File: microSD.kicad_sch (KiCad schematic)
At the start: 3 parts, among them J16 Micro_SD_Card_Det

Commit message: commit
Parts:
- added JP31: SolderJumper_2_Open, iclr:SmallerSolderJP, symbol Jumper:SolderJumper_2_Open
- added Q1: PMOS, Package_TO_SOT_SMD:SOT-723, symbol Simulation_SPICE:PMOS
- added R39: 1k, Resistor_SMD:R_0402_1005Metric, symbol Device:R_Small
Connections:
- net +3V3: now also JP31.1 (A), Q1.3 (S); no longer C10.1, J16.4 (VDD)
- net GND: now also R39.1
- new net: C10.1, J16.4 (VDD), JP31.2 (B), Q1.1 (D)
- new net SD_Pow: Q1.2 (G), R39.2
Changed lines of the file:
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@@
 (kicad_sch (version 20230121) (generator eeschema)
   (paper "A4")
+  (junction (at 108.204 59.69) (diameter 0) (color 0 0 0 0)
+  )
+  (junction (at 99.822 54.102) (diameter 0) (color 0 0 0 0)
+  )
   (junction (at 104.902 101.6) (diameter 0) (color 0 0 0 0)
   )
   (junction (at 99.822 66.04) (diameter 0) (color 0 0 0 0)
+  )
+  (junction (at 99.822 64.77) (diameter 0) (color 0 0 0 0)
   )
   (no_connect (at 116.332 83.82))
   (no_connect (at 116.332 66.04))
+  (wire (pts (xy 99.822 64.77) (xy 87.376 64.77))
+    (stroke (width 0) (type default))
+  )
+  (wire (pts (xy 87.376 54.102) (xy 99.822 54.102))
+    (stroke (width 0) (type default))
+  )
   (wire (pts (xy 115.062 68.58) (xy 116.332 68.58))
     (stroke (width 0) (type default))
@@
     (stroke (width 0) (type default))
   )
+  (wire (pts (xy 87.376 56.134) (xy 87.376 54.102))
+    (stroke (width 0) (type default))
+  )
   (wire (pts (xy 99.822 66.04) (xy 99.822 73.66))
     (stroke (width 0) (type default))
@@
     (stroke (width 0) (type default))
   )
+  (wire (pts (xy 99.822 53.086) (xy 99.822 54.102))
+    (stroke (width 0) (type default))
+  )
   (wire (pts (xy 101.092 101.6) (xy 104.902 101.6))
     (stroke (width 0) (type default))
@@
     (stroke (width 0) (type default))
   )
+  (wire (pts (xy 107.442 59.69) (xy 108.204 59.69))
+    (stroke (width 0) (type default))
+  )
   (wire (pts (xy 108.712 86.36) (xy 108.712 101.6))
     (stroke (width 0) (type default))
@@
     (stroke (width 0) (type default))
   )
+  (wire (pts (xy 108.204 59.69) (xy 109.347 59.69))
+    (stroke (width 0) (type default))
+  )
+  (wire (pts (xy 87.376 64.77) (xy 87.376 63.754))
+    (stroke (width 0) (type default))
+  )
+  (wire (pts (xy 99.822 54.102) (xy 99.822 54.61))
+    (stroke (width 0) (type default))
+  )
   (wire (pts (xy 159.512 88.9) (xy 162.052 88.9))
     (stroke (width 0) (type default))
+  )
+  (hierarchical_label "SD_Pow" (shape input) (at 109.347 59.69 0) (fields_autoplaced)
+    (effects (font (size 1.27 1.27)) (justify left))
   )
   (hierarchical_label "VSPI_SCLK" (shape input) (at 115.062 76.2 180) (fields_autoplaced)
@@
     )
   )
+  (symbol (lib_id "power:GND") (at 108.204 64.77 0) (unit 1)
+    (in_bom yes) (on_board yes) (dnp no) (fields_autoplaced)
+    (property "Reference" "#PWR085" (at 108.204 71.12 0)
+      (effects (font (size 1.27 1.27)) hide)
+    )
+    (property "Value" "GND" (at 110.109 66.4738 0)
+      (effects (font (size 1.27 1.27)) (justify left) hide)
+    )
+    (property "Footprint" "" (at 108.204 64.77 0)
+      (effects (font (size 1.27 1.27)) hide)
+    )
+    (property "Datasheet" "" (at 108.204 64.77 0)
+      (effects (font (size 1.27 1.27)) hide)
+    )
+    (pin "1")
+    (instances
+      (project "Ricardo-Stark"
+        (path "/7db990e4-92e1-4f99-b4d2-435bbec1ba83/cbb4aecb-b4d4-4eab-8e16-74accf8129be"
+          (reference "#PWR030") (unit 1)
+        )
+      )
+    )
+  )
   (symbol (lib_id "power:+3.3V") (at 104.902 92.71 0) (unit 1)
     (in_bom yes) (on_board yes) (dnp no) (fields_autoplaced)
@@
     )
   )
-  (symbol (lib_id "power:+3.3V") (at 99.822 64.77 0) (unit 1)
-    (in_bom yes) (on_board yes) (dnp no) (fields_autoplaced)
-    (property "Reference" "#PWR0157" (at 99.822 68.58 0)
-      (effects (font (size 1.27 1.27)) hide)
-    )
-    (property "Value" "+3.3V" (at 99.822 59.69 0)
-      (effects (font (size 1.27 1.27)))
-    )
-    (property "Footprint" "" (at 99.822 64.77 0)
-      (effects (font (size 1.27 1.27)) hide)
-    )
-    (property "Datasheet" "" (at 99.822 64.77 0)
-      (effects (font (size 1.27 1.27)) hide)
-    )
-    (pin "1")
-    (instances
-      (project "sensorboard"
-        (path "/26801cfb-b53b-4a6a-a2f4-5f4986565765/f50ea3f6-9887-4dc3-9ec9-7a0fb1ee7721"
-          (reference "#PWR0157") (unit 1)
-        )
-      )
-      (project "Ricardo-Stark"
-        (path "/7db990e4-92e1-4f99-b4d2-435bbec1ba83/cbb4aecb-b4d4-4eab-8e16-74accf8129be"
-          (reference "#PWR0169") (unit 1)
+  (symbol (lib_id "Jumper:SolderJumper_2_Open") (at 87.376 59.944 270) (unit 1)
+    (in_bom yes) (on_board yes) (dnp no)
+    (property "Reference" "JP31" (at 82.296 59.944 0)
+      (effects (font (size 1.27 1.27)))
+    )
+    (property "Value" "SolderJumper_2_Open" (at 55.626 42.164 0)
+      (effects (font (size 1.27 1.27)) hide)
+    )
+    (property "Footprint" "iclr:SmallerSolderJP" (at 87.376 59.944 0)
+      (effects (font (size 1.27 1.27)) hide)
+    )
+    (property "Datasheet" "~" (at 87.376 59.944 0)
+      (effects (font (size 1.27 1.27)) hide)
+    )
+    (pin "1")
+    (pin "2")
+    (instances
+      (project "sensorboard - Copy"
+        (path "/26801cfb-b53b-4a6a-a2f4-5f4986565765/00000000-0000-0000-0000-000061b9f0c0"
+          (reference "JP31") (unit 1)
+        )
+      )
+      (project "Ricardo-Stark"
+        (path "/7db990e4-92e1-4f99-b4d2-435bbec1ba83/249a9f46-b59f-4de1-97d1-386ac76339a5"
+          (reference "JP27") (unit 1)
+        )
+        (path "/7db990e4-92e1-4f99-b4d2-435bbec1ba83/cbb4aecb-b4d4-4eab-8e16-74accf8129be"
+          (reference "JP3") (unit 1)
         )
       )
@@
         )
       )
+    )
+  )
+  (symbol (lib_id "power:+3.3V") (at 99.822 53.086 0) (unit 1)
+    (in_bom yes) (on_board yes) (dnp no) (fields_autoplaced)
+    (property "Reference" "#PWR0159" (at 99.822 56.896 0)
+      (effects (font (size 1.27 1.27)) hide)
+    )
+    (property "Value" "+3.3V" (at 99.822 48.006 0)
+      (effects (font (size 1.27 1.27)))
+    )
+    (property "Footprint" "" (at 99.822 53.086 0)
+      (effects (font (size 1.27 1.27)) hide)
+    )
+    (property "Datasheet" "" (at 99.822 53.086 0)
+      (effects (font (size 1.27 1.27)) hide)
+    )
+    (pin "1")
+    (instances
+      (project "sensorboard"
+        (path "/26801cfb-b53b-4a6a-a2f4-5f4986565765/f50ea3f6-9887-4dc3-9ec9-7a0fb1ee7721"
+          (reference "#PWR0159") (unit 1)
+        )
+      )
+      (project "Ricardo-Stark"
+        (path "/7db990e4-92e1-4f99-b4d2-435bbec1ba83/cbb4aecb-b4d4-4eab-8e16-74accf8129be"
+          (reference "#PWR031") (unit 1)
+        )
+      )
+    )
+  )
+  (symbol (lib_id "Device:R_Small") (at 108.204 62.23 180) (unit 1)
+    (in_bom yes) (on_board yes) (dnp no)
+    (property "Reference" "R39" (at 104.775 62.3601 0)
+      (effects (font (size 1.27 1.27)))
+    )
+    (property "Value" "1k" (at 104.775 64.897 0)
+      (effects (font (size 1.27 1.27)))
+    )
+    (property "Footprint" "Resistor_SMD:R_0402_1005Metric" (at 108.204 62.23 0)
+      (effects (font (size 1.27 1.27)) hide)
+    )
+    (property "Datasheet" "~" (at 108.204 62.23 0)
+      (effects (font (size 1.27 1.27)) hide)
+    )
+    (pin "1")
+    (pin "2")
+    (instances
+      (project "Ricardo-Stark"
+        (path "/7db990e4-92e1-4f99-b4d2-435bbec1ba83/cbb4aecb-b4d4-4eab-8e16-74accf8129be"
+          (reference "R14") (unit 1)
+        )
+      )
+    )
+  )
+  (symbol (lib_id "Simulation_SPICE:PMOS") (at 102.362 59.69 180) (unit 1)
+    (in_bom yes) (on_board yes) (dnp no) (fields_autoplaced)
+    (property "Reference" "Q1" (at 96.012 58.42 0)
+      (effects (font (size 1.27 1.27)) (justify left))
+    )
+    (property "Value" "PMOS" (at 96.012 60.96 0)
+      (effects (font (size 1.27 1.27)) (justify left))
+    )
+    (property "Footprint" "Package_TO_SOT_SMD:SOT-723" (at 97.282 62.23 0)
+      (effects (font (size 1.27 1.27)) hide)
+    )
+    (property "Datasheet" "https://ngspice.sourceforge.io/docs/ngspice-manual.pdf" (at 102.362 46.99 0)
+      (effects (font (size 1.27 1.27)) hide)
+    )
+    (property "Sim.Device" "PMOS" (at 102.362 42.545 0)
+      (effects (font (size 1.27 1.27)) hide)
+    )
+    (property "Sim.Type" "VDMOS" (at 102.362 40.64 0)
+      (effects (font (size 1.27 1.27)) hide)
+    )
+    (property "Sim.Pins" "1=D 2=G 3=S" (at 102.362 44.45 0)
+      (effects (font (size 1.27 1.27)) hide)
+    )
+    (pin "2")
+    (pin "3")
+    (pin "1")
+    (instances
+      (project "Ricardo-Stark"
+        (path "/7db990e4-92e1-4f99-b4d2-435bbec1ba83/cbb4aecb-b4d4-4eab-8e16-74accf8129be"
+          (reference "Q1") (unit 1)
+        )
+      )

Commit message: added silkscreen
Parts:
- renumbered R39 to R14
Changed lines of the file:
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@@
   (symbol (lib_id "power:GND") (at 108.204 64.77 0) (unit 1)
     (in_bom yes) (on_board yes) (dnp no) (fields_autoplaced)
-    (property "Reference" "#PWR085" (at 108.204 71.12 0)
+    (property "Reference" "#PWR030" (at 108.204 71.12 0)
       (effects (font (size 1.27 1.27)) hide)
     )
@@
   (symbol (lib_id "Device:R_Small") (at 108.204 62.23 180) (unit 1)
     (in_bom yes) (on_board yes) (dnp no)
-    (property "Reference" "R39" (at 104.775 62.3601 0)
-      (effects (font (size 1.27 1.27)))
-    )
+    (property "Reference" "R14" (at 104.775 62.3601 0)
+      (effects (font (size 1.27 1.27)))
+    )

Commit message: changed sd mosfet footprint
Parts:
- Q1: footprint Package_TO_SOT_SMD:SOT-723 -> Package_TO_SOT_SMD:TSOT-23
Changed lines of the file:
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@@
 			)
 		)
-		(property "Footprint" "Package_TO_SOT_SMD:SOT-723"
+		(property "Footprint" "Package_TO_SOT_SMD:TSOT-23"
 			(at 97.282 62.23 0)
 			(effects
@@
 			)
 		)
-		(property "Datasheet" "https://ngspice.sourceforge.io/docs/ngspice-manual.pdf"
+		(property "Datasheet" "https://www.diodes.com/assets/Datasheets/DMP3099L.pdf"
 			(at 102.362 46.99 0)
 			(effects

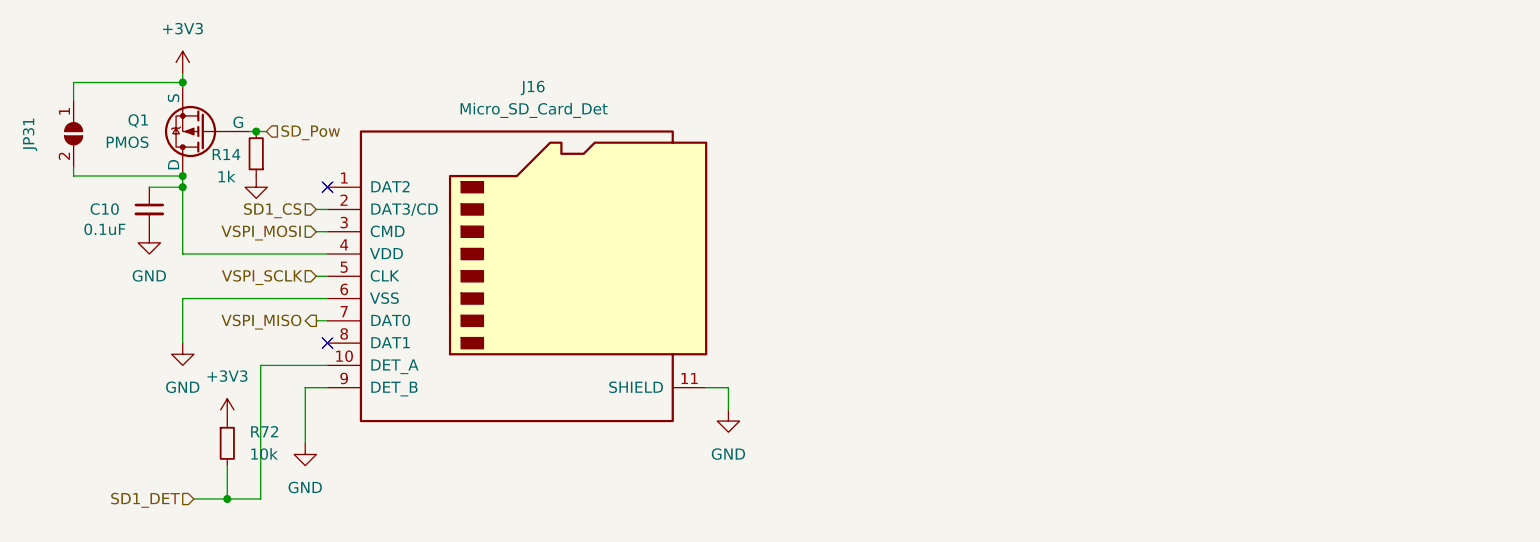
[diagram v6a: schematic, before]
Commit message: Changed sd card holder
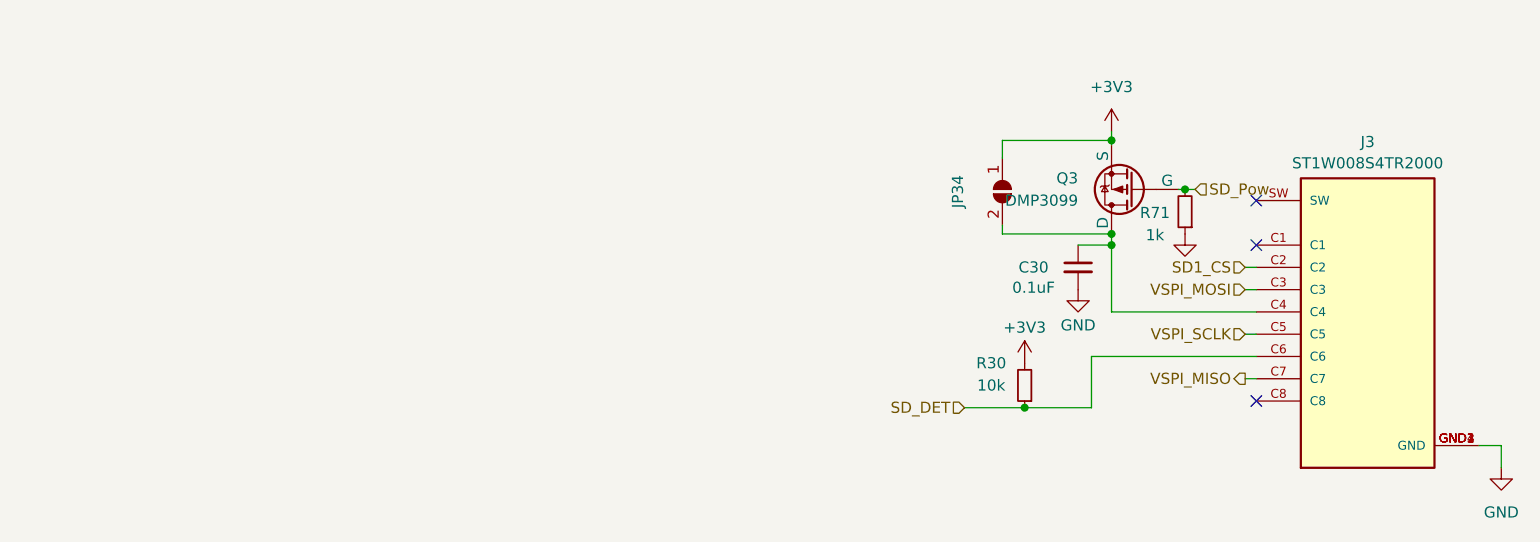
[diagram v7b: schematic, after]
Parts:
- removed C10: 0.1uF, Capacitor_SMD:C_0402_1005Metric, symbol Device:C_Small
- removed J16: Micro_SD_Card_Det, Connector_Card:microSD_HC_Hirose_DM3AT-SF-PEJM5, symbol Connector:Micro_SD_Card_Det
- removed JP31: SolderJumper_2_Open, iclr:SmallerSolderJP, symbol Jumper:SolderJumper_2_Open
- removed Q1: PMOS, Package_TO_SOT_SMD:TSOT-23, symbol Simulation_SPICE:PMOS
- removed R14: 1k, Resistor_SMD:R_0402_1005Metric, symbol Device:R_Small
- removed R72: 10k, Resistor_SMD:R_0402_1005Metric, symbol Device:R_Small
- added C30: 0.1uF, Capacitor_SMD:C_0402_1005Metric, symbol Device:C_Small
- added J3: ST1W008S4TR2000, iclr:JAE_ST1W008S4TR2000, symbol iclr:ST1W008S4TR2000
- added JP34: SolderJumper_2_Open, iclr:SmallerSolderJP, symbol Jumper:SolderJumper_2_Open
- added Q3: DMP3099, Package_TO_SOT_SMD:SOT-23, symbol Simulation_SPICE:PMOS
- added R30: 10k, Resistor_SMD:R_0402_1005Metric, symbol Device:R_Small
- added R71: 1k, Resistor_SMD:R_0402_1005Metric, symbol Device:R_Small
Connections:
- net +3V3: now also JP34.1 (A), Q3.3 (S), R30.2
- net GND: now also C30.2, J3.GND1 (GND), J3.GND2 (GND), J3.GND3 (GND), J3.GND4 (GND), R71.1
- net SD1_CS: now also J3.C2
- net SD_Pow: now also Q3.2 (G), R71.2
- net VSPI_MISO: now also J3.C7
- net VSPI_MOSI: now also J3.C3
- net VSPI_SCLK: now also J3.C5
- new net: C30.1, J3.C4, JP34.2 (B), Q3.1 (D)
- new net SD_DET: J3.C6, R30.1
- no-connect marks 2 -> 3

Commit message: Fixed sd det
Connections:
- net GND: now also J3.C6
- net SD_DET: now also J3.SW; no longer J3.C6
- no-connect marks 3 -> 2
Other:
- moved on the sheet: C30, JP34, Q3, R30, R71
